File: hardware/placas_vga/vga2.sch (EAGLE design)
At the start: 3 parts

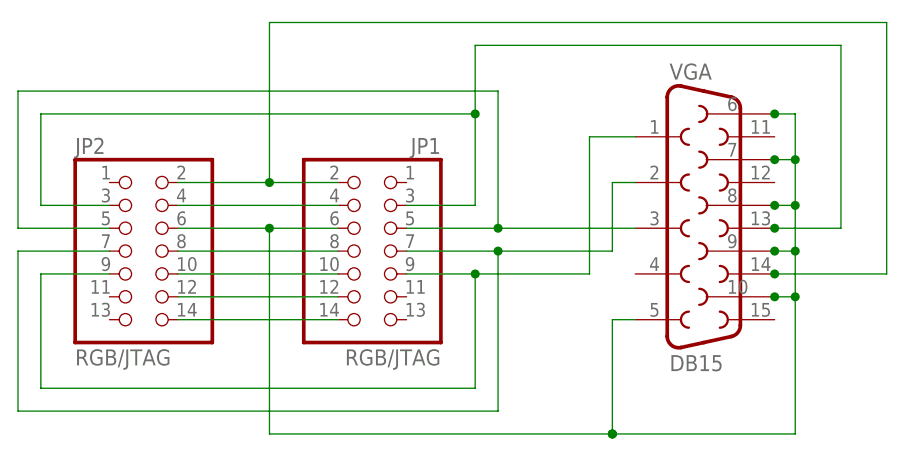
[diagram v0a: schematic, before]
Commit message: Rectificación fallo pinout
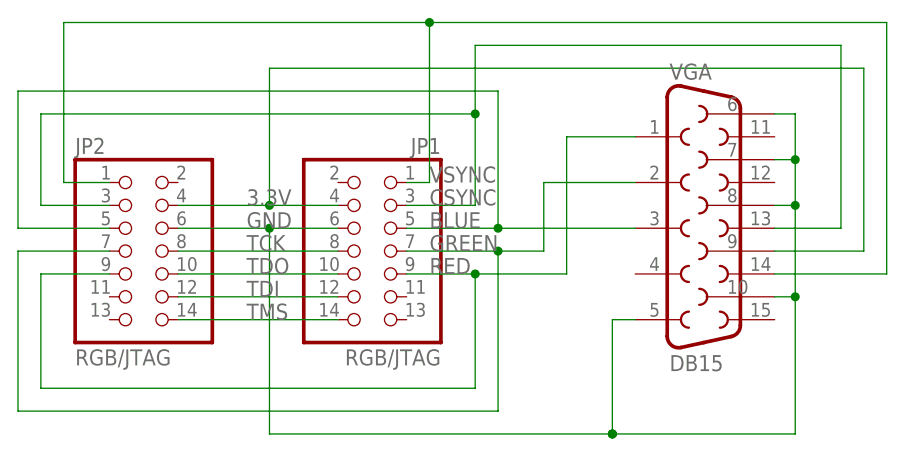
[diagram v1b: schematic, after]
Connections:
- net N$10 renamed RED
- net N$15 renamed BLUE
- net N$2 renamed TCK
- net N$3 renamed TDO
- net N$4 renamed TDI
- net N$5 renamed TMS
- net N$6 renamed GREEN
- net N$8 renamed CSYNC
- removed net N$1: JP1.4, JP2.4
- removed net N$13: JP1.6, JP2.6, VGA.10, VGA.5, VGA.6, VGA.7, VGA.8, VGA.9
- removed net N$7: JP1.2, JP2.2, VGA.14
- new net 3.3V: JP1.4, JP2.4, VGA.9
- new net GND: JP1.6, JP2.6, VGA.10, VGA.5, VGA.6, VGA.7, VGA.8
- new net VSYNC: JP1.1, JP2.1, VGA.14
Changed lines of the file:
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@@
 <?xml version="1.0" encoding="utf-8"?>
 <!DOCTYPE eagle SYSTEM "eagle.dtd">
-<eagle version="6.5.0">
+<eagle version="7.3.0">
 <drawing>
 <settings>
@@
 </busses>
 <nets>
-<net name="N$7" class="0">
-<segment>
-<wire x1="25.4" y1="73.66" x2="17.78" y2="73.66" width="0.1524" layer="91"/>
-<wire x1="17.78" y1="73.66" x2="17.78" y2="91.44" width="0.1524" layer="91"/>
-<wire x1="17.78" y1="91.44" x2="86.36" y2="91.44" width="0.1524" layer="91"/>
+<net name="VSYNC" class="0">
+<segment>
+<wire x1="-5.08" y1="91.44" x2="35.56" y2="91.44" width="0.1524" layer="91"/>
+<wire x1="35.56" y1="91.44" x2="86.36" y2="91.44" width="0.1524" layer="91"/>
 <wire x1="86.36" y1="91.44" x2="86.36" y2="63.5" width="0.1524" layer="91"/>
-<wire x1="73.66" y1="63.5" x2="73.914" y2="63.5" width="0.1524" layer="91"/>
 <pinref part="VGA" gate="G$1" pin="14"/>
 <wire x1="73.914" y1="63.5" x2="86.36" y2="63.5" width="0.1524" layer="91"/>
-<junction x="73.914" y="63.5"/>
-<pinref part="JP1" gate="A" pin="2"/>
-<pinref part="JP2" gate="A" pin="2"/>
-<wire x1="7.62" y1="73.66" x2="17.78" y2="73.66" width="0.1524" layer="91"/>
-<junction x="17.78" y="73.66"/>
-</segment>
-</net>
-<net name="N$8" class="0">
+<pinref part="JP2" gate="A" pin="1"/>
+<wire x1="0" y1="73.66" x2="-5.08" y2="73.66" width="0.1524" layer="91"/>
+<wire x1="-5.08" y1="73.66" x2="-5.08" y2="91.44" width="0.1524" layer="91"/>
+<pinref part="JP1" gate="A" pin="1"/>
+<wire x1="33.02" y1="73.66" x2="35.56" y2="73.66" width="0.1524" layer="91"/>
+<wire x1="35.56" y1="73.66" x2="35.56" y2="91.44" width="0.1524" layer="91"/>
+<junction x="35.56" y="91.44"/>
+<label x="35.56" y="73.66" size="1.778" layer="95"/>
+</segment>
+</net>
+<net name="CSYNC" class="0">
 <segment>
 <wire x1="33.02" y1="71.12" x2="40.64" y2="71.12" width="0.1524" layer="91"/>
@@
 <wire x1="40.64" y1="88.9" x2="81.28" y2="88.9" width="0.1524" layer="91"/>
 <wire x1="81.28" y1="88.9" x2="81.28" y2="68.58" width="0.1524" layer="91"/>
-<wire x1="73.66" y1="68.58" x2="73.914" y2="68.58" width="0.1524" layer="91"/>
 <pinref part="VGA" gate="G$1" pin="13"/>
 <wire x1="73.914" y1="68.58" x2="81.28" y2="68.58" width="0.1524" layer="91"/>
-<junction x="73.914" y="68.58"/>
 <pinref part="JP1" gate="A" pin="3"/>
 <pinref part="JP2" gate="A" pin="3"/>
@@
 <wire x1="-7.62" y1="81.28" x2="40.64" y2="81.28" width="0.1524" layer="91"/>
 <junction x="40.64" y="81.28"/>
-</segment>
-</net>
-<net name="N$13" class="0">
+<label x="35.56" y="71.12" size="1.778" layer="95"/>
+</segment>
+</net>
+<net name="GND" class="0">
 <segment>
 <wire x1="25.4" y1="68.58" x2="17.78" y2="68.58" width="0.1524" layer="91"/>
 <wire x1="17.78" y1="45.72" x2="17.78" y2="68.58" width="0.1524" layer="91"/>
-<wire x1="73.66" y1="81.28" x2="73.914" y2="81.28" width="0.1524" layer="91"/>
 <wire x1="73.914" y1="81.28" x2="76.2" y2="81.28" width="0.1524" layer="91"/>
 <wire x1="76.2" y1="81.28" x2="76.2" y2="76.2" width="0.1524" layer="91"/>
 <wire x1="76.2" y1="76.2" x2="76.2" y2="71.12" width="0.1524" layer="91"/>
-<wire x1="76.2" y1="71.12" x2="76.2" y2="66.04" width="0.1524" layer="91"/>
-<wire x1="76.2" y1="66.04" x2="76.2" y2="60.96" width="0.1524" layer="91"/>
+<wire x1="76.2" y1="71.12" x2="76.2" y2="60.96" width="0.1524" layer="91"/>
 <wire x1="76.2" y1="60.96" x2="76.2" y2="45.72" width="0.1524" layer="91"/>
 <wire x1="76.2" y1="45.72" x2="55.88" y2="45.72" width="0.1524" layer="91"/>
-<wire x1="73.66" y1="76.2" x2="73.914" y2="76.2" width="0.1524" layer="91"/>
 <junction x="76.2" y="76.2"/>
 <wire x1="73.914" y1="76.2" x2="76.2" y2="76.2" width="0.1524" layer="91"/>
-<wire x1="73.66" y1="71.12" x2="73.914" y2="71.12" width="0.1524" layer="91"/>
 <junction x="76.2" y="71.12"/>
 <wire x1="73.914" y1="71.12" x2="76.2" y2="71.12" width="0.1524" layer="91"/>
-<wire x1="73.66" y1="66.04" x2="73.914" y2="66.04" width="0.1524" layer="91"/>
-<junction x="76.2" y="66.04"/>
-<wire x1="73.914" y1="66.04" x2="76.2" y2="66.04" width="0.1524" layer="91"/>
-<wire x1="73.66" y1="60.96" x2="73.914" y2="60.96" width="0.1524" layer="91"/>
 <junction x="76.2" y="60.96"/>
-<pinref part="VGA" gate="G$1" pin="5"/>
 <wire x1="73.914" y1="60.96" x2="76.2" y2="60.96" width="0.1524" layer="91"/>
-<wire x1="58.42" y1="58.42" x2="55.88" y2="58.42" width="0.1524" layer="91"/>
-<wire x1="55.88" y1="58.42" x2="55.88" y2="45.72" width="0.1524" layer="91"/>
 <junction x="55.88" y="45.72"/>
 <pinref part="VGA" gate="G$1" pin="7"/>
-<junction x="73.914" y="76.2"/>
 <pinref part="VGA" gate="G$1" pin="8"/>
-<junction x="73.914" y="71.12"/>
-<pinref part="VGA" gate="G$1" pin="9"/>
-<junction x="73.914" y="66.04"/>
 <pinref part="VGA" gate="G$1" pin="10"/>
-<junction x="73.914" y="60.96"/>
 <pinref part="VGA" gate="G$1" pin="6"/>
-<junction x="73.914" y="81.28"/>
 <junction x="55.88" y="45.72"/>
 <wire x1="17.78" y1="45.72" x2="55.88" y2="45.72" width="0.1524" layer="91"/>
@@
 <wire x1="7.62" y1="68.58" x2="17.78" y2="68.58" width="0.1524" layer="91"/>
 <junction x="17.78" y="68.58"/>
-</segment>
-</net>
-<net name="N$15" class="0">
+<label x="15.24" y="68.58" size="1.778" layer="95"/>
+<pinref part="VGA" gate="G$1" pin="5"/>
+<wire x1="58.42" y1="58.42" x2="55.88" y2="58.42" width="0.1524" layer="91"/>
+<wire x1="55.88" y1="58.42" x2="55.88" y2="45.72" width="0.1524" layer="91"/>
+</segment>
+</net>
+<net name="BLUE" class="0">
 <segment>
 <pinref part="VGA" gate="G$1" pin="3"/>
@@
 <wire x1="43.18" y1="83.82" x2="43.18" y2="68.58" width="0.1524" layer="91"/>
 <junction x="43.18" y="68.58"/>
-</segment>
-</net>
-<net name="N$1" class="0">
+<label x="35.56" y="68.58" size="1.778" layer="95"/>
+</segment>
+</net>
+<net name="3.3V" class="0">
 <segment>
 <pinref part="JP2" gate="A" pin="4"/>
 <pinref part="JP1" gate="A" pin="4"/>
-<wire x1="7.62" y1="71.12" x2="25.4" y2="71.12" width="0.1524" layer="91"/>
-</segment>
-</net>
-<net name="N$2" class="0">
+<wire x1="7.62" y1="71.12" x2="17.78" y2="71.12" width="0.1524" layer="91"/>
+<label x="15.24" y="71.12" size="1.778" layer="95"/>
+<wire x1="17.78" y1="71.12" x2="25.4" y2="71.12" width="0.1524" layer="91"/>
+<wire x1="73.914" y1="66.04" x2="83.82" y2="66.04" width="0.1524" layer="91"/>
+<wire x1="83.82" y1="66.04" x2="83.82" y2="86.36" width="0.1524" layer="91"/>
+<wire x1="83.82" y1="86.36" x2="17.78" y2="86.36" width="0.1524" layer="91"/>
+<wire x1="17.78" y1="86.36" x2="17.78" y2="71.12" width="0.1524" layer="91"/>
+<junction x="17.78" y="71.12"/>
+<pinref part="VGA" gate="G$1" pin="9"/>
+</segment>
+</net>
+<net name="TCK" class="0">
 <segment>
 <pinref part="JP2" gate="A" pin="8"/>
 <pinref part="JP1" gate="A" pin="8"/>
 <wire x1="7.62" y1="66.04" x2="25.4" y2="66.04" width="0.1524" layer="91"/>
-</segment>
-</net>
-<net name="N$3" class="0">
+<label x="15.24" y="66.04" size="1.778" layer="95"/>
+</segment>
+</net>
+<net name="TDO" class="0">
 <segment>
 <pinref part="JP2" gate="A" pin="10"/>
 <pinref part="JP1" gate="A" pin="10"/>
 <wire x1="7.62" y1="63.5" x2="25.4" y2="63.5" width="0.1524" layer="91"/>
-</segment>
-</net>
-<net name="N$4" class="0">
+<label x="15.24" y="63.5" size="1.778" layer="95"/>
+</segment>
+</net>
+<net name="TDI" class="0">
 <segment>
 <pinref part="JP1" gate="A" pin="12"/>
 <pinref part="JP2" gate="A" pin="12"/>
 <wire x1="25.4" y1="60.96" x2="7.62" y2="60.96" width="0.1524" layer="91"/>
-</segment>
-</net>
-<net name="N$5" class="0">
+<label x="15.24" y="60.96" size="1.778" layer="95"/>
+</segment>
+</net>
+<net name="TMS" class="0">
 <segment>
 <pinref part="JP2" gate="A" pin="14"/>
 <pinref part="JP1" gate="A" pin="14"/>
 <wire x1="7.62" y1="58.42" x2="25.4" y2="58.42" width="0.1524" layer="91"/>
-</segment>
-</net>
-<net name="N$10" class="0">
+<label x="15.24" y="58.42" size="1.778" layer="95"/>
+</segment>
+</net>
+<net name="RED" class="0">
 <segment>
 <pinref part="JP2" gate="A" pin="9"/>
@@
 <wire x1="-7.62" y1="50.8" x2="40.64" y2="50.8" width="0.1524" layer="91"/>
 <wire x1="33.02" y1="63.5" x2="40.64" y2="63.5" width="0.1524" layer="91"/>
-<wire x1="40.64" y1="63.5" x2="53.34" y2="63.5" width="0.1524" layer="91"/>
-<wire x1="53.34" y1="63.5" x2="53.34" y2="78.74" width="0.1524" layer="91"/>
+<wire x1="40.64" y1="63.5" x2="50.8" y2="63.5" width="0.1524" layer="91"/>
+<wire x1="50.8" y1="63.5" x2="50.8" y2="78.74" width="0.1524" layer="91"/>
 <pinref part="VGA" gate="G$1" pin="1"/>
-<wire x1="53.34" y1="78.74" x2="58.42" y2="78.74" width="0.1524" layer="91"/>
+<wire x1="50.8" y1="78.74" x2="58.42" y2="78.74" width="0.1524" layer="91"/>
 <pinref part="JP1" gate="A" pin="9"/>
 <wire x1="40.64" y1="50.8" x2="40.64" y2="63.5" width="0.1524" layer="91"/>
 <junction x="40.64" y="63.5"/>
-</segment>
-</net>
-<net name="N$6" class="0">
+<label x="35.56" y="63.5" size="1.778" layer="95"/>
+</segment>
+</net>
+<net name="GREEN" class="0">
 <segment>
 <pinref part="JP2" gate="A" pin="7"/>
@@
 <wire x1="-10.16" y1="66.04" x2="-10.16" y2="48.26" width="0.1524" layer="91"/>
 <wire x1="33.02" y1="66.04" x2="43.18" y2="66.04" width="0.1524" layer="91"/>
-<wire x1="43.18" y1="66.04" x2="55.88" y2="66.04" width="0.1524" layer="91"/>
-<wire x1="55.88" y1="66.04" x2="55.88" y2="73.66" width="0.1524" layer="91"/>
+<wire x1="43.18" y1="66.04" x2="48.26" y2="66.04" width="0.1524" layer="91"/>
+<wire x1="48.26" y1="66.04" x2="48.26" y2="73.66" width="0.1524" layer="91"/>
 <pinref part="VGA" gate="G$1" pin="2"/>
-<wire x1="55.88" y1="73.66" x2="58.42" y2="73.66" width="0.1524" layer="91"/>
+<wire x1="48.26" y1="73.66" x2="58.42" y2="73.66" width="0.1524" layer="91"/>
 <pinref part="JP1" gate="A" pin="7"/>
 <wire x1="-10.16" y1="48.26" x2="43.18" y2="48.26" width="0.1524" layer="91"/>
 <wire x1="43.18" y1="48.26" x2="43.18" y2="66.04" width="0.1524" layer="91"/>
 <junction x="43.18" y="66.04"/>
-</segment>
-</net>
+<label x="35.56" y="66.04" size="1.778" layer="95"/>
+</segment>
+</net>
